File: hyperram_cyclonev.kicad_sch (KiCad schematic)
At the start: 59 parts

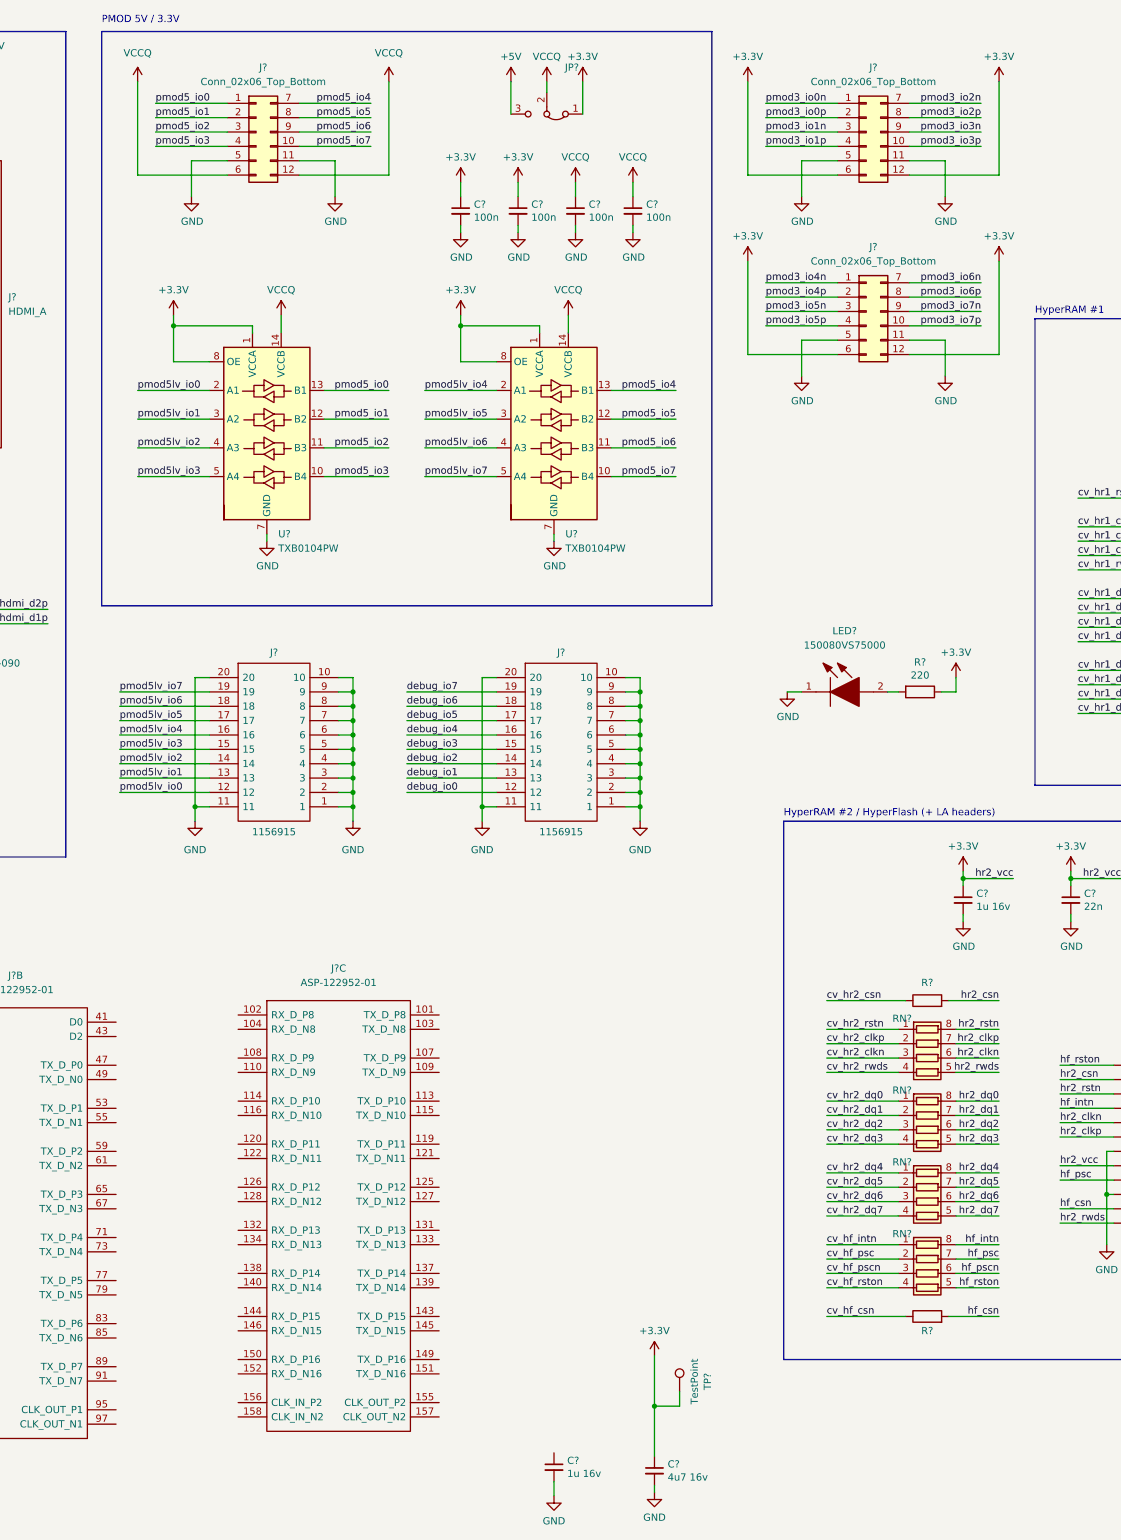
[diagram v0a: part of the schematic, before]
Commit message: Added DC/DC converter to get 5V for PMOD and HDMI from 12V. Changed two TXB0104 to one TXB0108 for PMOD 5V.
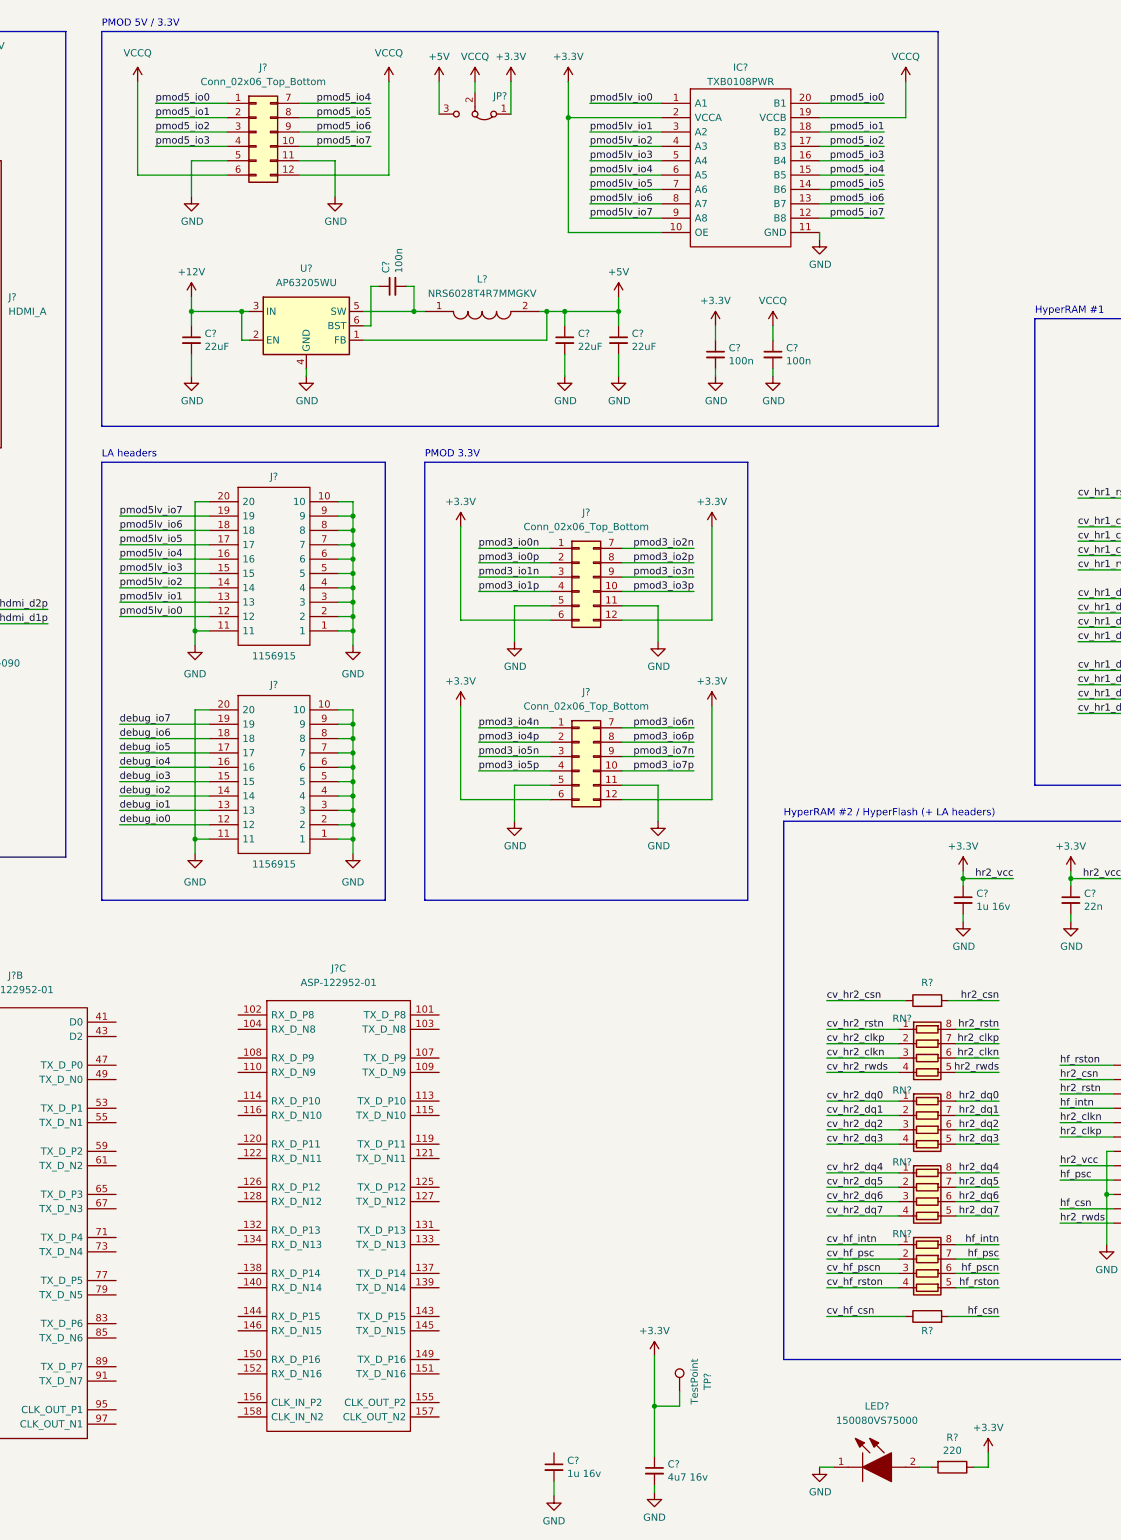
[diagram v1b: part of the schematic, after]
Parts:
- removed C? (x3): 100n, Capacitor_SMD:C_0402_1005Metric_Pad0.74x0.62mm_HandSolder, symbol Device:C_Small
- removed U? (x2): TXB0104PW, Package_SO:TSSOP-14_4.4x5mm_P0.65mm, symbol Logic_LevelTranslator:TXB0104PW
- added C? (x2): 100n, Capacitor_SMD:C_0603_1608Metric_Pad1.08x0.95mm_HandSolder, symbol Device:C_Small
- added C? (x3): 22uF, Capacitor_SMD:C_0805_2012Metric_Pad1.18x1.45mm_HandSolder, symbol Device:C_Small
- added IC?: TXB0108PWR, SOP65P640X120-20N, symbol hyperram_cyclonev:TXB0108PWR
- added L?: NRS6028T4R7MMGKV, NRS6028T4R7MMGK, symbol hyperram_cyclonev:NRS6028T4R7MMGKV
- added U?: AP63205WU, Package_TO_SOT_SMD:TSOT-23-6, symbol Regulator_Switching:AP63205WU
- C?: footprint Capacitor_SMD:C_0402_1005Metric_Pad0.74x0.62mm_HandSolder -> Capacitor_SMD:C_0603_1608Metric_Pad1.08x0.95mm_HandSolder; Part CGA3E2X7R1H223K080AA -> 06033C104KAT2A
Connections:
- net +12V: now also C?.1, U?.2 (EN), U?.3 (IN)
- net +3V3: now also IC?.10 (OE), IC?.2 (VCCA)
- net +5V: now also C?.1, C?.1, L?.2, U?.1 (FB)
- net GND: now also C?.2, C?.2, C?.2, C?.2, IC?.11 (GND), U?.4 (GND)
- net VCCQ: now also C?.1, IC?.19 (VCCB)
- net pmod5_io0: now also IC?.20 (B1)
- net pmod5_io1: now also IC?.18 (B2)
- net pmod5_io2: now also IC?.17 (B3)
- net pmod5_io3: now also IC?.16 (B4)
- net pmod5_io4: now also IC?.15 (B5)
- net pmod5_io5: now also IC?.14 (B6)
- net pmod5_io6: now also IC?.13 (B7)
- net pmod5_io7: now also IC?.12 (B8)
- net pmod5lv_io0: now also IC?.1 (A1)
- net pmod5lv_io1: now also IC?.3 (A2)
- net pmod5lv_io2: now also IC?.4 (A3)
- net pmod5lv_io3: now also IC?.5 (A4)
- net pmod5lv_io4: now also IC?.6 (A5)
- net pmod5lv_io5: now also IC?.7 (A6)
- net pmod5lv_io6: now also IC?.8 (A7)
- net pmod5lv_io7: now also IC?.9 (A8)
- new net: C?.1, U?.6 (BST)
- new net: C?.2, L?.1, U?.5 (SW)
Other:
- note added: "LA headers"
- note added: "PMOD 3.3V"
- moved on the sheet: C?, J?, JP?, LED?, R?

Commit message: Updated schematics, made connections between PMODs, HyperBUS devices, Debug Header, QSPI NOR Flash, HDMI and HSMC.
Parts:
- removed C?: 4u7 16v, Capacitor_SMD:C_0805_2012Metric_Pad1.18x1.45mm_HandSolder, symbol Device:C_Small
- removed C?: 1u 16v, Capacitor_SMD:C_0805_2012Metric_Pad1.18x1.45mm_HandSolder, symbol Device:C_Small
- removed IC?: W25Q32JVSSIQ_TR, SOIC127P790X216-8N, symbol hyperram_asic:W25Q32JVSSIQ_TR
- removed IC? (x2): S27KL0641DABHI020, BGA24C100P5X5_600X800X100, symbol hyperram_asic:S27KL0641DABHI020
- removed J? (x4): 1156915, 1156915, symbol hyperram_asic:1156915
- removed TP?: TestPoint, TestPoint:TestPoint_Pad_D1.0mm, symbol Connector:TestPoint
- added IC3: S26KL128SDABHI020, BGA24C100P5X5_600X800X100, symbol hyperram_cyclonev:S26KL128SDABHI020
- added IC4: W25Q32JVSSIQ_TR, SOIC127P790X216-8N, symbol hyperram_cyclonev:W25Q32JVSSIQ_TR
- added IC5: S27KL0641DABHI020, BGA24C100P5X5_600X800X100, symbol hyperram_cyclonev:S27KL0641DABHI020
- added J3, J4, J8, J9: 1156915, 1156915, symbol hyperram_cyclonev:1156915
- added TP1, TP2, TP3, TP4: TestPoint, TestPoint:TestPoint_Pad_D1.0mm, symbol Connector:TestPoint
- gave numbers to parts that had none: 50
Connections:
- net +12V: now also TP3.1
- net +3V3: now also IC3.B4 (VCC), IC3.D1 (VCCQ_1), IC3.E4 (VCCQ_2), IC4.8 (VCC), IC5.B4 (VCC), IC5.D1 (VCCQ_1), IC5.E4 (VCCQ_2), TP1.1
- net +5V: now also TP2.1
- net GND: now also IC3.B3 (VSS), IC3.C1 (VSSQ_1), IC3.E5 (VSSQ_2), IC4.4 (GND), IC5.B3 (VSS), IC5.C1 (VSSQ_1), IC5.E5 (VSSQ_2), J3.1, J3.10, J3.11, J3.2, J3.20, J3.3, J3.4, J3.5, J3.6, J3.7, J3.8, J3.9, J4.1, J4.10, J4.11, J4.2, J4.20, J4.3, J4.4, J4.5, J4.6, J4.7, J4.8, J4.9, J8.1, J8.10, J8.11, J8.2, J8.20, J8.3, J8.4, J8.5, J8.6, J8.7, J8.8, J8.9, J9.1, J9.10, J9.11, J9.2, J9.20, J9.3, J9.4, J9.5, J9.6, J9.7, J9.8, J9.9, TP4.1
- net cec: now also J1.158 (CLK_IN_N2)
- net cv_hf_csn: now also J1.41 (D0)
- net cv_hf_intn: now also J1.49 (TX_D_N0)
- net cv_hf_psc: now also J1.78 (RX_D_P5)
- net cv_hf_pscn: now also J1.80 (RX_D_N5)
- net cv_hf_rston: now also J1.47 (TX_D_P0)
- net cv_hr1_clkn: now also J1.85 (TX_D_N6)
- net cv_hr1_clkp: now also J1.83 (TX_D_P6)
- net cv_hr1_csn: now also J1.53 (TX_D_P1)
- net cv_hr1_dq0: now also J1.79 (TX_D_N5)
- net cv_hr1_dq1: now also J1.77 (TX_D_P5)
- net cv_hr1_dq2: now also J1.73 (TX_D_N4)
- net cv_hr1_dq3: now also J1.71 (TX_D_P4)
- net cv_hr1_dq4: now also J1.67 (TX_D_N3)
- net cv_hr1_dq5: now also J1.65 (TX_D_P3)
- net cv_hr1_dq6: now also J1.61 (TX_D_N2)
- net cv_hr1_dq7: now also J1.59 (TX_D_P2)
- net cv_hr1_rstn: now also J1.89 (TX_D_P7)
- net cv_hr1_rwds: now also J1.55 (TX_D_N1)
- net cv_hr2_clkn: now also J1.74 (RX_D_N4)
- net cv_hr2_clkp: now also J1.72 (RX_D_P4)
- net cv_hr2_csn: now also J1.42 (D1)
- net cv_hr2_dq0: now also J1.68 (RX_D_N3)
- net cv_hr2_dq1: now also J1.66 (RX_D_P3)
- net cv_hr2_dq2: now also J1.62 (RX_D_N2)
- net cv_hr2_dq3: now also J1.60 (RX_D_P2)
- net cv_hr2_dq4: now also J1.56 (RX_D_N1)
- net cv_hr2_dq5: now also J1.54 (RX_D_P1)
- net cv_hr2_dq6: now also J1.50 (RX_D_N0)
- net cv_hr2_dq7: now also J1.48 (RX_D_P0)
- net cv_hr2_rstn: now also J1.43 (D2)
- net cv_hr2_rwds: now also J1.44 (D3)
- net ddc_clk_lv: now also J1.157 (CLK_OUT_N2)
- net ddc_dat_lv: now also J1.155 (CLK_OUT_P2)
- net debug_io0: now also J1.91 (TX_D_N7), J4.12
- net debug_io1: now also J1.95 (CLK_OUT_P1), J4.13
- net debug_io2: now also J1.97 (CLK_OUT_N1), J4.14
- net debug_io3: now also J1.101 (TX_D_P8), J4.15
- net debug_io4: now also J1.103 (TX_D_N8), J4.16
- net debug_io5: now also J1.107 (TX_D_P9), J4.17
- net debug_io6: now also J1.109 (TX_D_N9), J4.18
- net debug_io7: now also J1.113 (TX_D_P10), IC4.7 (IO3), J4.19
- net flash_clk: now also J1.125 (TX_D_P12), IC4.6 (CLK)
- net flash_csb: now also J1.127 (TX_D_N12), IC4.1 (/CS)
- net flash_io0: now also J1.121 (TX_D_N11), IC4.5 (DI(IO0))
- net flash_io1: now also J1.119 (TX_D_P11), IC4.2 (DO(IO1))
- net flash_io2: now also J1.115 (TX_D_N10), IC4.3 (IO2)
- net hdmi_clkn: now also J1.151 (TX_D_N16)
- net hdmi_clkp: now also J1.149 (TX_D_P16)
- net hdmi_d0n: now also J1.145 (TX_D_N15)
- net hdmi_d0p: now also J1.143 (TX_D_P15)
- net hdmi_d1n: now also J1.139 (TX_D_N14)
- net hdmi_d1p: now also J1.137 (TX_D_P14)
- net hdmi_d2n: now also J1.133 (TX_D_N13)
- net hdmi_d2p: now also J1.131 (TX_D_P13)
- net hf_csn: now also IC3.C2 (CS#), J9.14
- net hf_intn: now also IC3.A5 (INT#), J9.12
- net hf_psc: now also IC3.B5 (PSC), J9.13
- net hf_pscn: now also IC3.C5 (PSC#)
- net hf_rston: now also IC3.A2 (RSTO#)
- net hpdet: now also J1.156 (CLK_IN_P2)
- net hr1_clkn: now also IC5.B1 (CK#)
- net hr1_clkp: now also IC5.B2 (CK)
- net hr1_csn: now also IC5.A3 (CS#)
- net hr1_dq0: now also IC5.D3 (DQ0)
- net hr1_dq1: now also IC5.D2 (DQ1)
- net hr1_dq2: now also IC5.C4 (DQ2)
- net hr1_dq3: now also IC5.D4 (DQ3)
- net hr1_dq4: now also IC5.D5 (DQ4)
- net hr1_dq5: now also IC5.E3 (DQ5)
- net hr1_dq6: now also IC5.E2 (DQ6)
- net hr1_dq7: now also IC5.E1 (DQ7)
- net hr1_rstn: now also IC5.A4 (RESET#)
- net hr1_rwds: now also IC5.C3 (RWDS)
- net hr2_clkn: now also IC3.B1 (CK#), J9.18
- net hr2_clkp: now also IC3.B2 (CK), J9.17
- net hr2_csn: now also IC3.A3 (DNU), J9.15
- net hr2_dq0: now also IC3.D3 (DQ0), J8.12
- net hr2_dq1: now also IC3.D2 (DQ1), J8.13
- net hr2_dq2: now also IC3.C4 (DQ2), J8.14
- net hr2_dq3: now also IC3.D4 (DQ3), J8.15
- net hr2_dq4: now also IC3.D5 (DQ4), J8.16
- net hr2_dq5: now also IC3.E3 (DQ5), J8.17
- net hr2_dq6: now also IC3.E2 (DQ6), J8.18
- net hr2_dq7: now also IC3.E1 (DQ7), J8.19
- net hr2_rstn: now also IC3.A4 (RESET#), J9.16
- net hr2_rwds: now also IC3.C3 (RWDS), J9.19
- net pmod3_io0n: now also J1.110 (RX_D_N9)
- net pmod3_io0p: now also J1.108 (RX_D_P9)
- net pmod3_io1n: now also J1.116 (RX_D_N10)
- net pmod3_io1p: now also J1.114 (RX_D_P10)
- net pmod3_io2n: now also J1.122 (RX_D_N11)
- net pmod3_io2p: now also J1.120 (RX_D_P11)
- net pmod3_io3n: now also J1.128 (RX_D_N12)
- net pmod3_io3p: now also J1.126 (RX_D_P12)
- net pmod3_io4n: now also J1.134 (RX_D_N13)
- net pmod3_io4p: now also J1.132 (RX_D_P13)
- net pmod3_io5n: now also J1.140 (RX_D_N14)
- net pmod3_io5p: now also J1.138 (RX_D_P14)
- net pmod3_io6n: now also J1.146 (RX_D_N15)
- net pmod3_io6p: now also J1.144 (RX_D_P15)
- net pmod3_io7n: now also J1.152 (RX_D_N16)
- net pmod3_io7p: now also J1.150 (RX_D_P16)
- net pmod5lv_io0: now also J1.84 (RX_D_P6), J3.12
- net pmod5lv_io1: now also J1.86 (RX_D_N6), J3.13
- net pmod5lv_io2: now also J1.90 (RX_D_P7), J3.14
- net pmod5lv_io3: now also J1.92 (RX_D_N7), J3.15
- net pmod5lv_io4: now also J1.96 (CLK_IN_P1), J3.16
- net pmod5lv_io5: now also J1.98 (CLK_IN_N1), J3.17
- net pmod5lv_io6: now also J1.102 (RX_D_P8), J3.18
- net pmod5lv_io7: now also J1.104 (RX_D_N8), J3.19
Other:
- moved on the sheet: J1B, J1C
